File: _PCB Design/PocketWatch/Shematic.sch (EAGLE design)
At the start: 44 parts, among them U2 ATTINY88-AU

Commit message: Changed Tube common to positive voltage. Changed to multiplexer design base (Frees up pins for motor control).
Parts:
- removed T1, T2, T3, T4: (no value), transistor:MMBT918LT1-NPN-SOT23-BEC
- added IC1: 74HC139D, 74xx-eu:74HC139D
- added Q1, Q2, Q3, Q4: BCX71SMD, transistor-pnp:BCX71SMD
- added SV4: (no value), con-lstb:MA05-1
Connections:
- net TG0_2 renamed T0_2
- net TG1_2 renamed T1_2
- net TG2_2 renamed T2_2
- net TG3_2 renamed T3_2
- removed net EN0: R5.1, U2.PA0_(ADC6/PCINT24)
- removed net EN1: R6.1, U2.PA1_(ADC7/PCINT25)
- removed net EN2: R7.1, U2.PA2_(PCINT26)
- removed net EN3: R8.1, U2.PA3_(PCINT27)
- removed net TG0: SV5.4, T1.C
- removed net TG1: SV5.3, T2.C
- removed net TG2: SV5.2, T3.C
- removed net TG3: SV5.1, T4.C
- new net LEDC0: IC1B.B, U2.PA2_(PCINT26)
- new net LEDC1: IC1B.A, U2.PA3_(PCINT27)
- new net N$10: IC1A.Y1, R6.1
- new net N$11: IC1A.Y2, R7.1
- new net N$13: IC1A.Y3, R8.1
- new net N$18: IC1B.Y3, R14.2
- new net N$8: IC1A.Y0, R5.1
- new net T0: Q1.C, SV5.4
- new net T1: Q2.C, SV5.3
- new net T2: Q3.C, SV5.2
- new net T3: Q4.C, SV5.1
- new net TC0: IC1A.A, U2.PA0_(ADC6/PCINT24)
- new net TC1: IC1A.B, U2.PA1_(ADC7/PCINT25)
- net GND: now also IC1A.G, IC1B.G; no longer AM.C, COLIN1.C, COLIN2.C, PM.C, T1.E, T2.E, T3.E, T4.E
- net N$1: now also Q4.B; no longer T4.B
- net N$15: now also IC1B.Y0, R17.2; no longer R14.2, R15.2, U2.PB0_(PCINT0/CLKO/ICP1)
- net N$16: now also IC1B.Y1, R16.2; no longer R17.2, U2.PB2_(PCINT2/!SS!/OC1B)
- net N$17: now also IC1B.Y2, R15.2; no longer R16.2, U2.PB1_(PCINT1/OC1A)
- net N$2: now also Q3.B; no longer T3.B
- net N$3: now also Q2.B; no longer T2.B
- net N$5: now also Q1.B; no longer T1.B
- net VCC: now also AM.C, COLIN1.C, COLIN2.C, PM.C, Q1.E, Q2.E, Q3.E, Q4.E
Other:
- moved on the sheet: AM, COLIN1, COLIN2, PM, R14, R15, R16, R17, R5, R6, R7, R8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

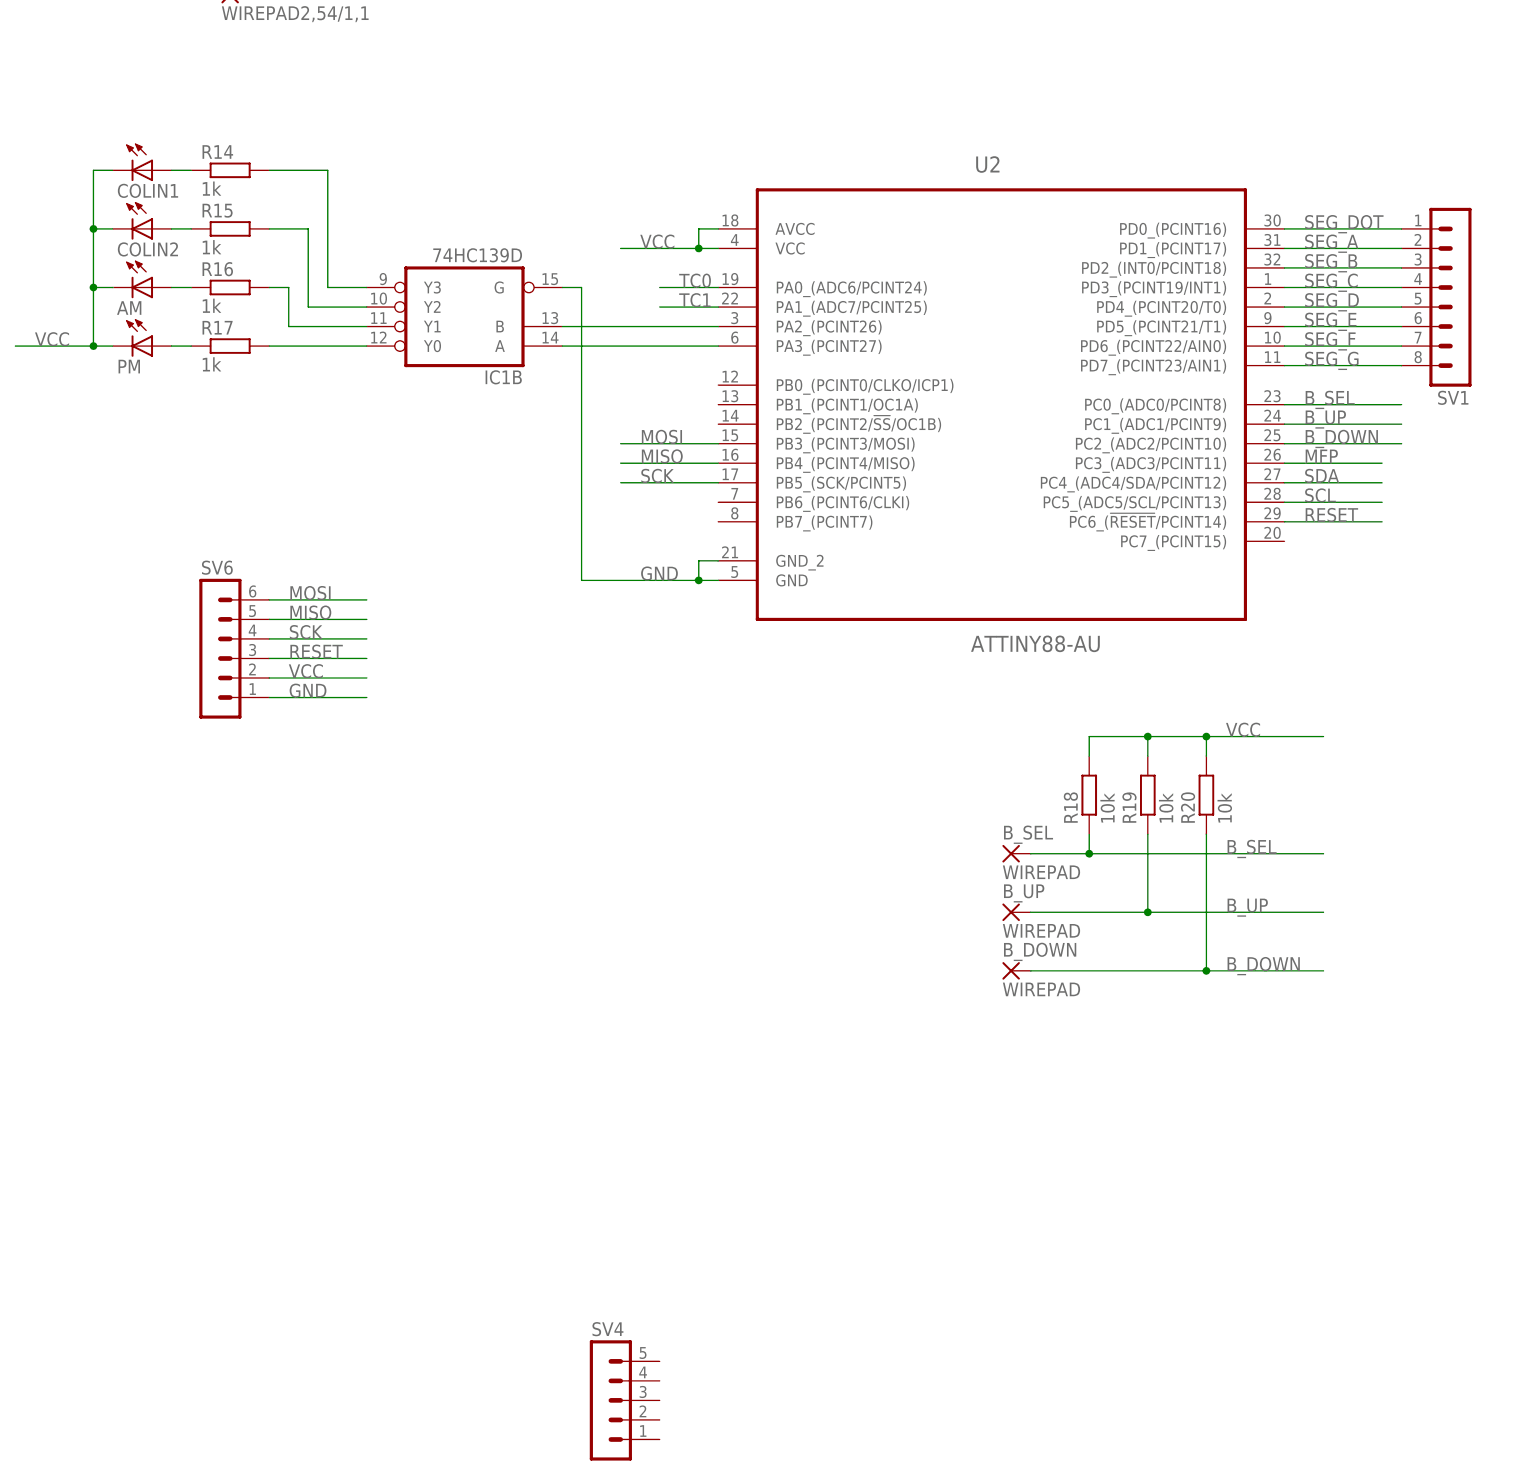
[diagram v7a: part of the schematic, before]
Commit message: Added Motor drive circuitry. Rearranged pin connections
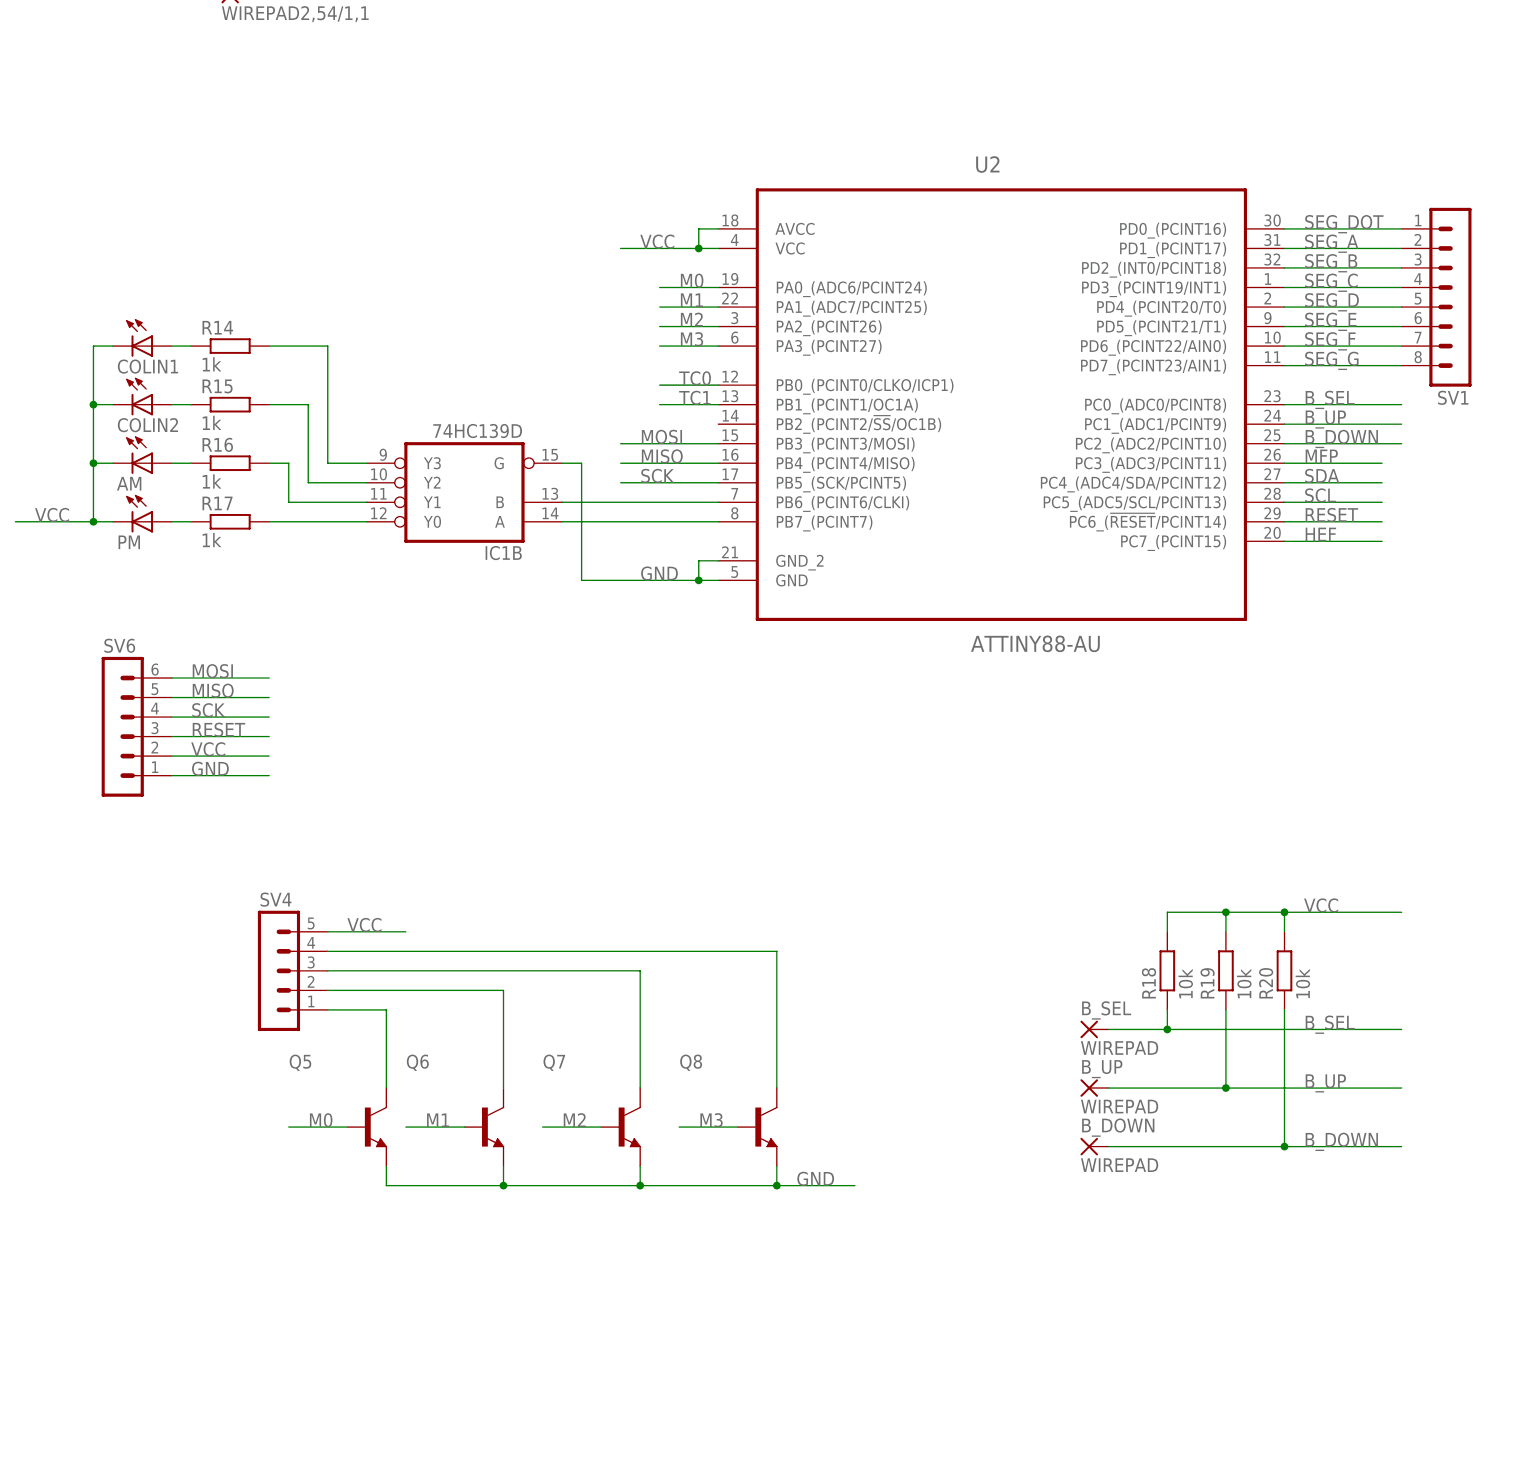
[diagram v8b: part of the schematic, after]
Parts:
- added Q5, Q6, Q7, Q8: BCX70SMD, transistor-npn:BCX70SMD
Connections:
- removed net LEDC0: IC1B.B, U2.PA2_(PCINT26)
- removed net LEDC1: IC1B.A, U2.PA3_(PCINT27)
- new net HEF: U2.PC7_(PCINT15)
- new net M0: Q5.B, U2.PA0_(ADC6/PCINT24)
- new net M1: Q6.B, U2.PA1_(ADC7/PCINT25)
- new net M2: Q7.B, U2.PA2_(PCINT26)
- new net M3: Q8.B, U2.PA3_(PCINT27)
- new net N$19: Q5.C, SV4.1
- new net N$20: Q6.C, SV4.2
- new net N$21: Q7.C, SV4.3
- new net N$22: Q8.C, SV4.4
- new net N$27: IC1B.B, U2.PB6_(PCINT6/CLKI)
- new net N$28: IC1B.A, U2.PB7_(PCINT7)
- net GND: now also Q5.E, Q6.E, Q7.E, Q8.E
- net TC0: now also U2.PB0_(PCINT0/CLKO/ICP1); no longer U2.PA0_(ADC6/PCINT24)
- net TC1: now also U2.PB1_(PCINT1/OC1A); no longer U2.PA1_(ADC7/PCINT25)
- net VCC: now also SV4.5
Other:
- moved on the sheet: AM, B_DOWN, B_SEL, B_UP, COLIN1, COLIN2, IC1B, PM, R14, R15, R16, R17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
